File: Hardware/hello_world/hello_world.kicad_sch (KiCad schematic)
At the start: 4 parts, among them SW1 SW_Push

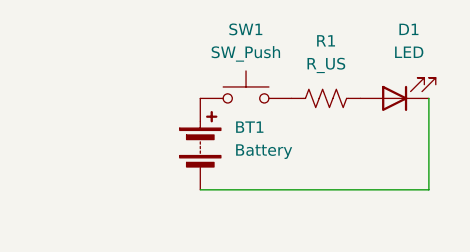
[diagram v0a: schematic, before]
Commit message: completed schematic and layout for the LED onboarding project
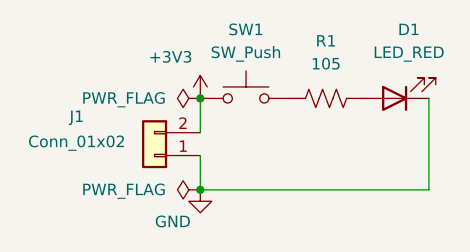
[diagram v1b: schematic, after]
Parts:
- removed BT1: Battery, symbol Device:Battery
- added J1: Conn_01x02, Connector_Molex:Molex_KK-254_AE-6410-02A_1x02_P2.54mm_Vertical, symbol Connector_Generic:Conn_01x02
- D1: value LED -> LED_RED; footprint (none) -> layout:LED_0603_Symbol_on_F.SilkS; MPN (none) -> 1825910-6; Notes (none) -> Red LED; Qty (none) -> 1
- R1: value R_US -> 105; footprint (none) -> Resistor_SMD:R_0603_1608Metric_Pad0.98x0.95mm_HandSolder; MPN (none) -> 022272021; Qty (none) -> 1
- SW1: footprint (none) -> Button_Switch_SMD:SW_DIP_SPSTx01_Slide_6.7x4.1mm_W6.73mm_P2.54mm_LowProfile_JPin; Qty (none) -> 1
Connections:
- net GND: now reaches D1.1 (K)
- net GND: now also J1.1 (Pin_1)
- net +3V3: now reaches SW1.1
- net +3V3: now also J1.2 (Pin_2)
